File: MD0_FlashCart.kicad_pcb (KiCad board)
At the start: 2 copper layers, 48.3 x 58.4 mm, 31 parts, among them J1 Conn_02x18_Odd_Even, J2 MM1134, Q1 Q_NMOS_GSD, U1 74LS174, U2 KM62256CLP, U3 AM29F040, U4 by ManCloud

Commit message: Finished Layout
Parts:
- removed BT1: CR2032_Holder, Battery:BatteryHolder_LINX_BAT-HLD-012-SMT
- removed C1, C2: 100n, Capacitor_SMD:C_0603_1608Metric
- removed H1, H2: MountingHole, MountingHole:MountingHole_4.5mm
- removed JP1, JP2: SolderJumper_3_Open, Jumper:SolderJumper-3_P1.3mm_Open_Pad1.0x1.5mm
- removed JP3, JP4: SolderJumper_2_Open, Jumper:SolderJumper-2_P1.3mm_Open_Pad1.0x1.5mm
- removed Q1: Q_NMOS_GSD, Package_TO_SOT_SMD:SOT-23
- removed R3: 1k, Resistor_SMD:R_0603_1608Metric
- removed R4, R5, R6: 10k, Resistor_SMD:R_0603_1608Metric
- J2: value MM1134 -> Conn_GameBoy_Cartridge; footprint Package_SO:SOIC-8_3.9x4.9mm_P1.27mm -> Gekkio_GameBoy:GameBoy_Cartridge
- moved U4 40.7 mm to (196.1, 84.1)
- moved R1 23.6 mm to (213.9, 77.0), turned to 90 degrees
- moved D3 21.0 mm to (212.1, 77.0), turned to 90 degrees
- moved D2 18.5 mm to (210.3, 77.0), turned to 90 degrees
- moved C5 18.3 mm to (168.1, 78.5)
- moved D1 15.9 mm to (208.5, 77.0), turned to 90 degrees
- moved J2 11.4 mm to (191.8, 70.4), turned to 180 degrees
- moved C4 7.14 mm to (203.7, 97.8), turned to -90 degrees
- moved U1 6.69 mm to (209.9, 85.3)
- moved C3 6.68 mm to (203.7, 82.0), turned to 90 degrees
- moved R2 5.98 mm to (189.0, 82.8), turned to -90 degrees
- moved U2 2.92 mm to (178.6, 84.6)
- moved D4 0.85 mm to (189.0, 79.5), turned to 90 degrees
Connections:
- C5 pad 1: VCCQ -> VCC
- D4 pad 1: ~{CE} -> ~{RAM_CE}
- J2 pad 1: GND -> VCC
- J2 pad 2: ~{RST} -> unconnected-(J2-PHI-Pad2)
- J2 pad 3: ~{CE_OUT} -> ~{WR}
- J2 pad 4: +BATT -> ~{RD}
- J2 pad 5: ~{RAM_CE} -> unconnected-(J2-~{CS}-Pad5)
- J2 pad 6: VCCQ -> A0
- J2 pad 7: ~{CE} -> A1
- J2 pad 8: VCC -> A2
- R2 pad 1: ~{CE} -> ~{RAM_CE}
- U1 pad 10: FLASH_A16 -> FLASH_A18
- U1 pad 2: FLASH_A13 -> FLASH_A15
- U1 pad 5: FLASH_A14 -> FLASH_A16
- U1 pad 7: FLASH_A15 -> FLASH_A17
- U2 pad 28: VCCQ -> VCC
- U3 pad 4: FLASH_A13 -> A13
- U3 pad 5: FLASH_A14 -> A14
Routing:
- net VCC: track 0.00 -> 142.8 mm, vias 0 -> 3
- net ~{RD}: track 0.00 -> 126.2 mm, vias 0 -> 6
- net ~{WR}: track 0.00 -> 107.8 mm, vias 0 -> 4
- net ~{RST}: track 0.00 -> 95.3 mm, vias 0 -> 4
- net D5: track 0.00 -> 93.2 mm, vias 0 -> 6
- net D2: track 0.00 -> 90.6 mm, vias 0 -> 5
- net D3: track 0.00 -> 90.5 mm, vias 0 -> 6
- net D0: track 0.00 -> 89.3 mm, vias 0 -> 5
- net D1: track 0.00 -> 88.9 mm, vias 0 -> 6
- net D4: track 0.00 -> 88.6 mm, vias 0 -> 5
- net A0: track 0.00 -> 85.9 mm, vias 0 -> 6
- net A12: track 0.00 -> 83.5 mm, vias 0 -> 5
- net A1: track 0.00 -> 81.9 mm, vias 0 -> 6
- net A14: track 0.00 -> 81.6 mm, vias 0 -> 4
- net A2: track 0.00 -> 79.8 mm, vias 0 -> 7
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- added copper zone on B.Cu, net GND
- added copper zone on F.Cu, net GND
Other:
- board size 48.3 x 58.4 mm -> 49.8 x 48 mm
- board text added: "MegaDuck FRAM_FlashCart"
- board text added: "v20250216"
- board text removed: "MegaDuck MD0_FlashCart"
- board text removed: "v20250213"

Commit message: Added Chiptypes - Some Cleanup
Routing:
- net VCC: track 142.8 -> 145.8 mm
- net A11: track 67.7 -> 68.3 mm
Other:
- board text added: "74LS174"
- board text added: "FLASH: M29F010 M29F040"
- board text added: "FRAM: FM1808"
- board text added: "MegaDuck FlashCart_FRAM"
- board text added: "v20250217"
- board text removed: "MegaDuck FRAM_FlashCart"
- board text removed: "v20250216"

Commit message: Updated to last version
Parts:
- added D5: D, Diode_SMD:D_0805_2012Metric_Pad1.15x1.40mm_HandSolder, F.Cu at (188.9, 83.2)
- D1, D2, D3, D4: footprint Diode_SMD:D_0603_1608Metric -> Diode_SMD:D_0805_2012Metric_Pad1.15x1.40mm_HandSolder
- moved R1 7.57 mm to (206.3, 77.2), turned to -90 degrees
- moved R2 3.80 mm to (189.0, 86.6)
- moved C5 3.55 mm to (171.1, 76.5), turned to 0 degrees
- moved C3 1.53 mm to (204.3, 80.6), turned to 0 degrees
- moved U4 1.33 mm to (196.5, 85.3)
- moved U1 1.27 mm to (208.7, 85.3)
- moved D1 0.33 mm to (208.2, 77.0)
- moved D3 0.31 mm to (212.4, 77.0)
- moved D4 0.31 mm to (188.9, 79.2)
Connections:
- J1 pad 5: ???1 -> ~{CE}
- J2 pad 5: unconnected-(J2-~{CS}-Pad5) -> ~{CE}
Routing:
- net ~{CE}: track 0.00 -> 88.6 mm, vias 0 -> 6
- net VCC: track 145.8 -> 154.0 mm
- net ~{RAM_CE}: track 11.6 -> 17.5 mm
- net unconnected-(J2-~{CS}-Pad5): track 3.81 -> 0.00 mm, vias 1 -> 0
- net A14: track 81.6 -> 85.1 mm
- net CLK: track 10.6 -> 12.0 mm
- net SRAM_A14: track 43.7 -> 42.4 mm
- net FLASH_A16: track 16.9 -> 15.7 mm
- net ~{RST}: track 95.3 -> 94.0 mm
- net FLASH_A15: track 12.6 -> 13.8 mm
- net D5: track 93.2 -> 92.0 mm
- net D4: track 88.6 -> 87.4 mm
- net FLASH_A18: track 26.7 -> 27.9 mm
- net FLASH_A17: track 21.5 -> 22.6 mm
- net D3: track 90.5 -> 89.3 mm
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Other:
- board text added: "v20250322"
- board text removed: "v20250217"

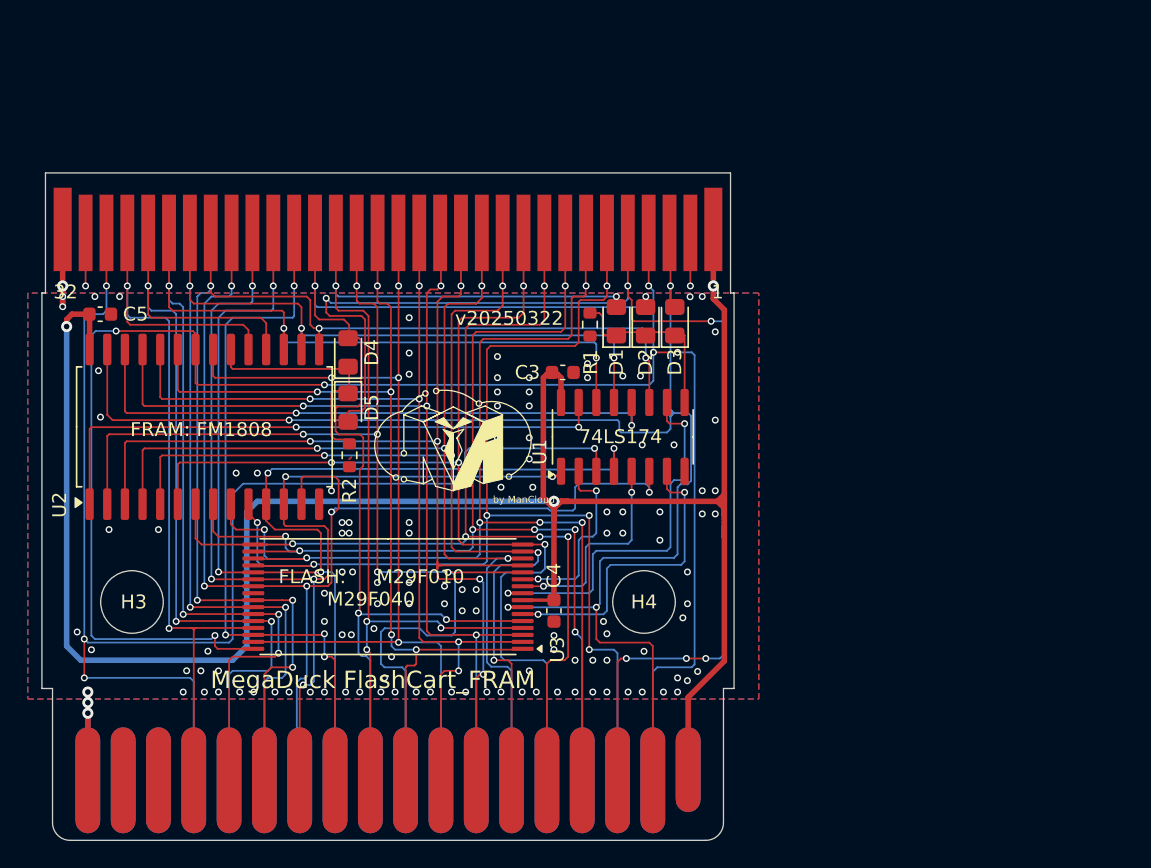
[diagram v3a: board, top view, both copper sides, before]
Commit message: Fixed !WR-pin to Flash
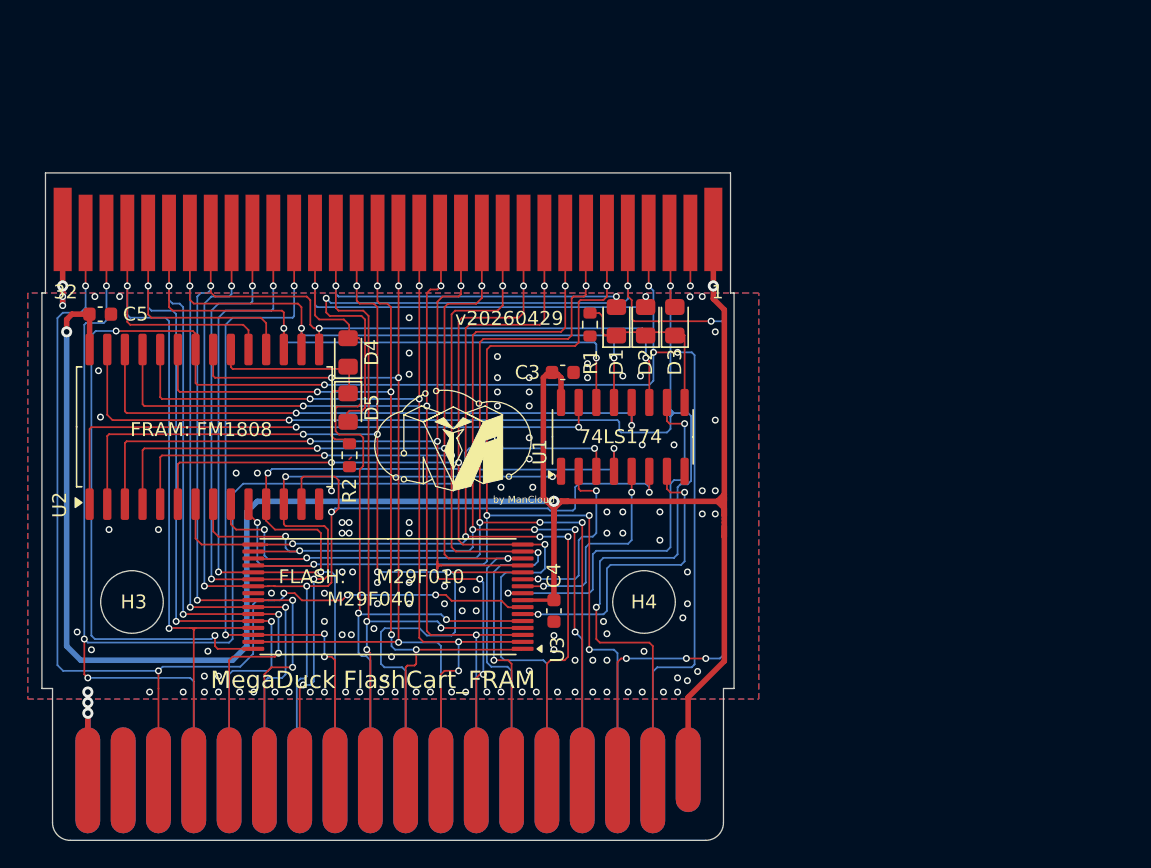
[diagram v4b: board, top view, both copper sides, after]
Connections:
- J1 pad 31: ???2 -> ~{FLASH_WR}
- J2 pad 31: unconnected-(J2-VIN-Pad31) -> ~{FLASH_WR}
- U3 pad 7: ~{WR} -> ~{FLASH_WR}
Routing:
- net ~{FLASH_WR}: track 0.00 -> 79.5 mm, vias 0 -> 5
- net ~{WR}: track 108.2 -> 100.8 mm, vias 4 -> 3
- net unconnected-(J2-VIN-Pad31): track 3.81 -> 0.00 mm, vias 1 -> 0
- net GND: track 20.0 -> 19.8 mm, vias 126 -> 127
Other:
- board text added: "v20260429"
- board text removed: "v20250322"
